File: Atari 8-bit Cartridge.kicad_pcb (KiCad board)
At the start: 2 copper layers, 55.9 x 59.3 mm, 13 parts, among them J2 Atari 8-bit Left Cartridge Co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, U0 27C128, U1 27C64, U2 74AHCT1G08

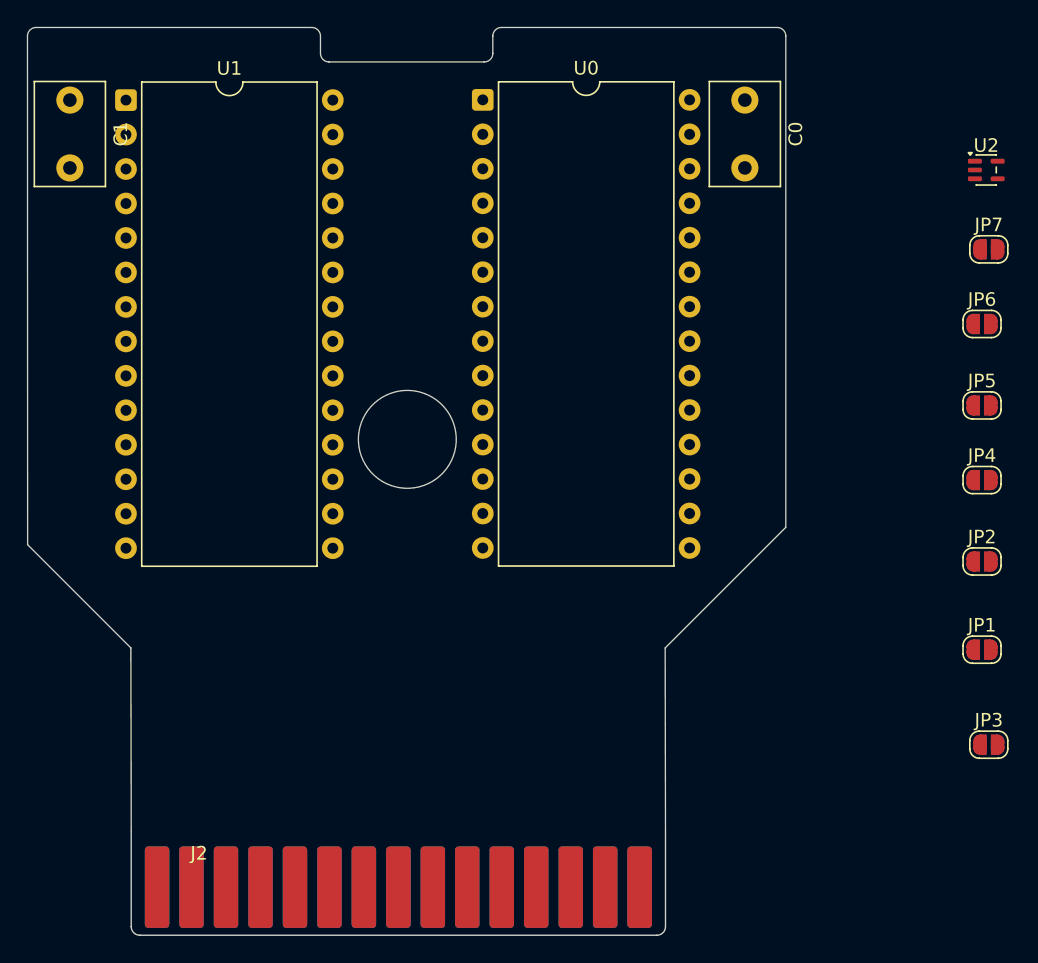
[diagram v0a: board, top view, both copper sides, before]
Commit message: Preliminary board layout.
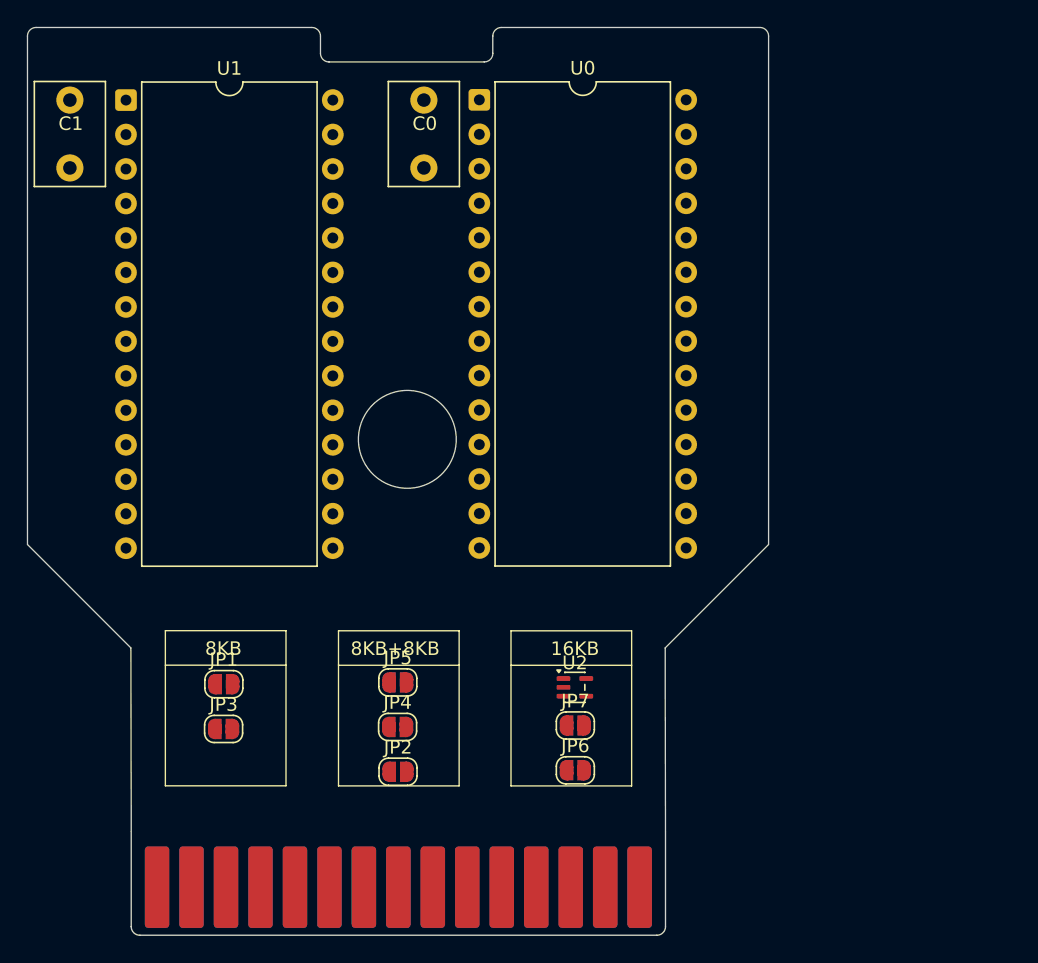
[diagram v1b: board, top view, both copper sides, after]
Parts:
- moved JP3 56.4 mm to (94.5, 108.8)
- moved JP1 55.9 mm to (94.5, 105.5)
- moved U2 48.7 mm to (120.3, 105.8)
- moved JP5 47.6 mm to (107.3, 105.4)
- moved JP4 46.8 mm to (107.3, 108.7)
- moved JP7 46.5 mm to (120.4, 108.6)
- moved JP2 45.7 mm to (107.3, 112.0)
- moved JP6 44.5 mm to (120.4, 111.9)
- moved C0 23.7 mm to (109.2, 62.5)
- moved U0 0.25 mm to (113.3, 62.5)
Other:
- board size 55.9 x 59.3 mm -> 54.6 x 59.3 mm
- board text added: "16KB"
- board text added: "8KB"
- board text added: "8KB+8KB"
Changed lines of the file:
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@@
 	(footprint "Jumper:SolderJumper-2_P1.3mm_Open_RoundedPad1.0x1.5mm"
 		(layer "F.Cu")
-		(at 150.35 90.5)
+		(at 107.283829 108.693226)
 		(descr "SMD Solder Jumper, 1x1.5mm, rounded Pads, 0.3mm gap, open")
 		(tags "solder jumper open")
@@
 	(footprint "Jumper:SolderJumper-2_P1.3mm_Open_RoundedPad1.0x1.5mm"
 		(layer "F.Cu")
-		(at 150.85 110)
+		(at 94.462247 108.840994)
 		(descr "SMD Solder Jumper, 1x1.5mm, rounded Pads, 0.3mm gap, open")
 		(tags "solder jumper open")
@@
 	(footprint "Capacitor_THT:C_Disc_D7.5mm_W5.0mm_P5.00mm"
 		(layer "F.Cu")
-		(at 132.873 62.5 -90)
+		(at 109.22 62.5 -90)
 		(descr "C, Disc series, Radial, pin pitch=5.00mm, diameter*width=7.5*5.0mm^2, Capacitor, http://www.vishay.com/docs/28535/vy2series.pdf")
 		(tags "C Disc series Radial pin pitch 5.00mm diameter 7.5mm width 5.0mm Capacitor")
 		(property "Reference" "C0"
-			(at 2.5 -3.75 90)
+			(at 1.738 -0.067 180)
 			(layer "F.SilkS")
 			(effects
@@
 	(footprint "Jumper:SolderJumper-2_P1.3mm_Open_RoundedPad1.0x1.5mm"
 		(layer "F.Cu")
-		(at 150.35 96.5)
+		(at 107.315 111.993)
 		(descr "SMD Solder Jumper, 1x1.5mm, rounded Pads, 0.3mm gap, open")
 		(tags "solder jumper open")
@@
 	(footprint "Jumper:SolderJumper-2_P1.3mm_Open_RoundedPad1.0x1.5mm"
 		(layer "F.Cu")
-		(at 150.85 73.5)
+		(at 120.381 108.585)
 		(descr "SMD Solder Jumper, 1x1.5mm, rounded Pads, 0.3mm gap, open")
 		(tags "solder jumper open")
@@
 	(footprint "Jumper:SolderJumper-2_P1.3mm_Open_RoundedPad1.0x1.5mm"
 		(layer "F.Cu")
-		(at 150.35 79)
+		(at 120.380999 111.886999)
 		(descr "SMD Solder Jumper, 1x1.5mm, rounded Pads, 0.3mm gap, open")
 		(tags "solder jumper open")
@@
 		)
 		(property "Value" "High+Low_Bank_Present"
-			(at 0 1.9 0)
+			(at 0.015 2.032 0)
 			(layer "F.Fab")
 			(effects
@@
 	(footprint "Jumper:SolderJumper-2_P1.3mm_Open_RoundedPad1.0x1.5mm"
 		(layer "F.Cu")
-		(at 150.35 85)
+		(at 107.3 105.41)
 		(descr "SMD Solder Jumper, 1x1.5mm, rounded Pads, 0.3mm gap, open")
 		(tags "solder jumper open")
@@
 	(footprint "Package_DIP:DIP-28_W15.24mm"
 		(layer "F.Cu")
-		(at 113.560473 62.483386)
+		(at 113.306473 62.483386)
 		(descr "28-lead though-hole mounted DIP package, row spacing 15.24mm (600 mils)")
 		(tags "THT DIP DIL PDIP 2.54mm 15.24mm 600mil")
@@
 		)
 		(point
-			(at 121.180473 78.993386)
+			(at 120.926473 78.993386)
 			(size 1.27)
 			(layer "F.Fab")
@@
 		(tags "C Disc series Radial pin pitch 5.00mm diameter 7.5mm width 5.0mm Capacitor")
 		(property "Reference" "C1"
-			(at 2.5 -3.75 90)
+			(at 1.738 -0.067 180)
 			(layer "F.SilkS")
 			(effects
@@
 			(at 2.5 3.75 90)
 			(layer "F.Fab")
+			(hide yes)
 			(effects
 				(font
@@
 			(at 5 -3.5 0)
 			(layer "F.SilkS")
+			(hide yes)
 			(effects
 				(font
@@
 		)
 		(property "Value" "Atari 8-bit Left Cartridge Connector"
-			(at 19.05 -7 0)
+			(at 21.086051 -5.864558 0)
 			(layer "F.Fab")
 			(effects
@@
 		)
 		(fp_text user "${REFERENCE}"
-			(at 16 -3.5 0)
+			(at 3.905165 -5.806902 0)
 			(layer "F.Fab")
 			(effects
@@
 	(footprint "Package_TO_SOT_SMD:SOT-353_SC-70-5"
 		(layer "F.Cu")
-		(at 150.6625 67.65)
+		(at 120.3445 105.776)
 		(descr "SOT, 5 Pin (https://home.jeita.or.jp/tsc/std-pdf/ED-7500A.pdf#page=171, JEDEC MO-203, variant AA, https://www.jedec.org/document_search?search_api_views_fulltext=MO-203)")
 		(tags "SOT TO_SOT_SMD SC-88A SOT-353 SC-70-5")
@@
 	(footprint "Jumper:SolderJumper-2_P1.3mm_Open_RoundedPad1.0x1.5mm"
 		(layer "F.Cu")
-		(at 150.35 103)
+		(at 94.481 105.54)
 		(descr "SMD Solder Jumper, 1x1.5mm, rounded Pads, 0.3mm gap, open")
 		(tags "solder jumper open")
@@
 		(embedded_fonts no)
 	)
+	(gr_rect
+		(start 90.17 101.6)
+		(end 99.06 113.03)
+		(radius 1)
+		(stroke
+			(width 0.1)
+			(type solid)
+		)
+		(fill no)
+		(layer "F.SilkS")
+	)
+	(gr_line
+		(start 90.17 104.14)
+		(end 99.06 104.14)
+		(stroke
+			(width 0.1)
+			(type solid)
+		)
+		(layer "F.SilkS")
+	)
+	(gr_rect
+		(start 102.927628 101.605382)
+		(end 111.817628 113.035382)
+		(radius 1)
+		(stroke
+			(width 0.1)
+			(type solid)
+		)
+		(fill no)
+		(layer "F.SilkS")
+	)
+	(gr_line
+		(start 102.927628 104.145382)
+		(end 111.817628 104.145382)
+		(stroke
+			(width 0.1)
+			(type solid)
+		)
+		(layer "F.SilkS")
+	)
+	(gr_rect
+		(start 115.639266 101.608707)
+		(end 124.529266 113.038707)
+		(radius 1)
+		(stroke
+			(width 0.1)
+			(type solid)
+		)
+		(fill no)
+		(layer "F.SilkS")
+	)
+	(gr_line
+		(start 115.639266 104.148707)
+		(end 124.529266 104.148707)
+		(stroke
+			(width 0.1)
+			(type solid)
+		)
+		(layer "F.SilkS")
+	)
 	(gr_arc
 		(start 80.01 57.785)
@@
 	)
 	(gr_line
-		(start 80.02 95.25)
+		(start 80.01 95.25)
 		(end 80.01 57.785)
 		(stroke
@@
 	(gr_line
 		(start 114.935 57.15)
-		(end 135.255 57.15)
+		(end 133.985 57.15)
 		(stroke
 			(width 0.05)
@@
 	(gr_line
 		(start 127 102.87)
-		(end 135.89 93.98)
+		(end 134.62 95.25)
 		(stroke
 			(width 0.05)
@@
 	)
 	(gr_arc
-		(start 135.255 57.15)
-		(mid 135.704013 57.335987)
-		(end 135.89 57.785)
+		(start 133.985 57.15)
+		(mid 134.434013 57.335987)
+		(end 134.62 57.785)
 		(stroke
 			(width 0.05)
@@
 	)
 	(gr_line
-		(start 135.89 57.785)
-		(end 135.89 93.98)
+		(start 134.62 57.785)
+		(end 134.62 95.25)
 		(stroke
 			(width 0.05)
@@
 		(layer "Edge.Cuts")
 	)
+	(gr_text "8KB"
+		(at 93.091 103.505 0)
+		(layer "F.SilkS")
+		(effects
+			(font
+				(size 1 1)
+				(thickness 0.15)
+			)
+			(justify left bottom)
+		)
+	)
+	(gr_text "8KB+8KB"
+		(at 103.816628 103.510382 0)
+		(layer "F.SilkS")
+		(effects
+			(font
+				(size 1 1)
+				(thickness 0.15)
+			)
+			(justify left bottom)
+		)
+	)
+	(gr_text "16KB"
+		(at 118.560266 103.513707 0)
+		(layer "F.SilkS")
+		(effects
+			(font
+				(size 1 1)
+				(thickness 0.15)
+			)
+			(justify left bottom)
+		)
+	)
 	(embedded_fonts no)
